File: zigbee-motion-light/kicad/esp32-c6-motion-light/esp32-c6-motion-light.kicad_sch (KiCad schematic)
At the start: 1 part, among them U1 XIAO-ESP32-C6-DIP

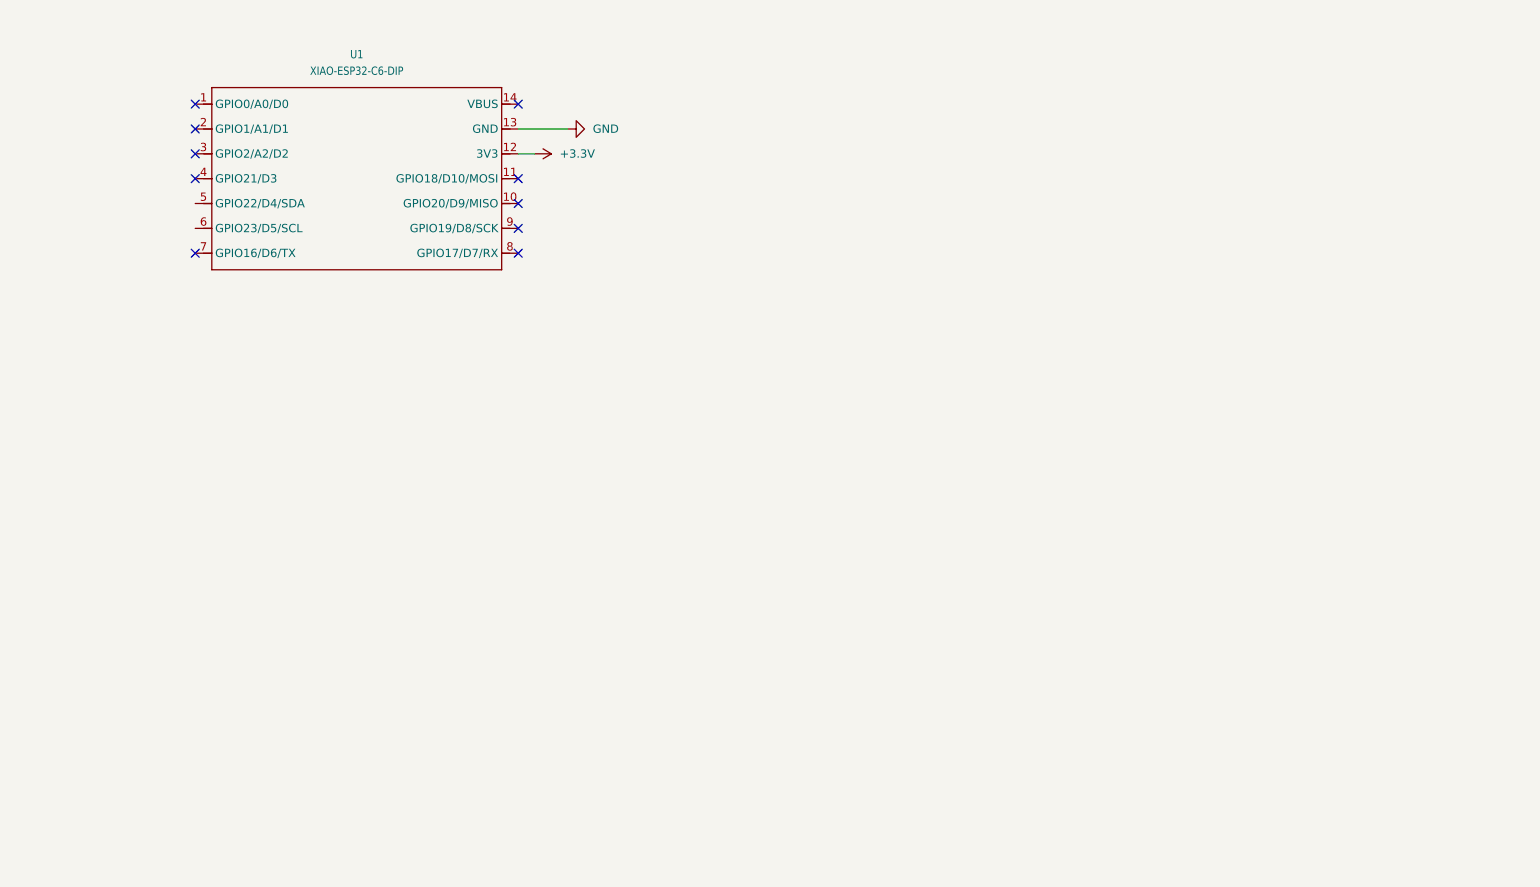
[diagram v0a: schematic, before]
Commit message: Add RP2040 component from EasyEDA and update KiCad project files
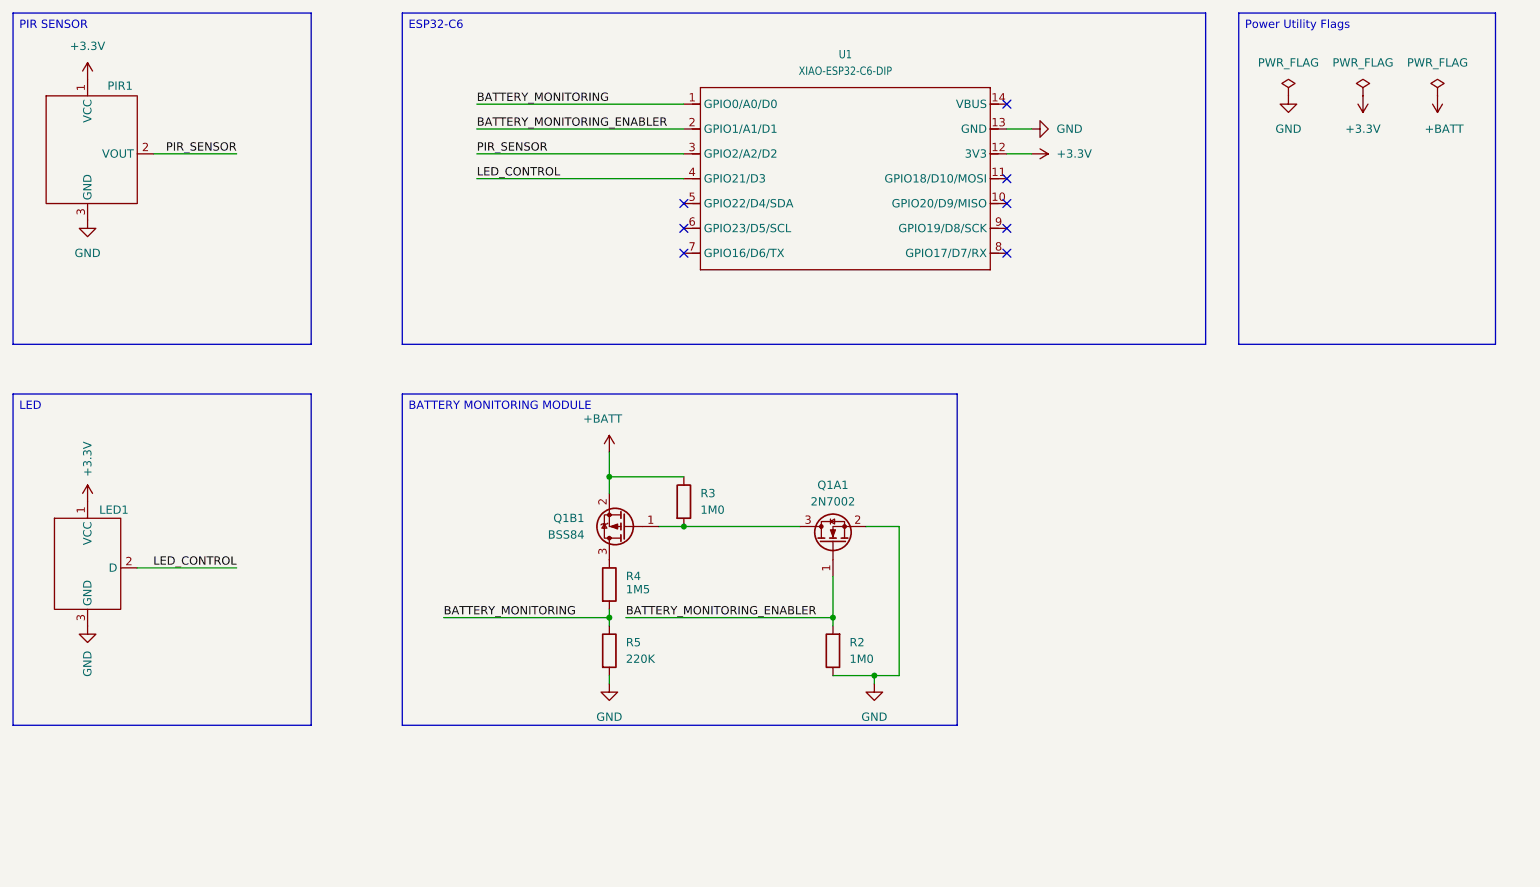
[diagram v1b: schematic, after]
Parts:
- added LED1: (no value), symbol New_Library:LED_CONNECTOR
- added PIR1: (no value), symbol New_Library:AM312_PIR
- added Q1A1: 2N7002, Package_TO_SOT_SMD:SOT-23, symbol Transistor_FET:2N7002
- added Q1B1: BSS84, Package_TO_SOT_SMD:SOT-23, symbol Transistor_FET:BSS84
- added R2, R3: 1M0, symbol Device:R
- added R4: 1M5, symbol Device:R
- added R5: 220K, symbol Device:R
- U1: footprint Library:XIAO-ESP32-C6-DIP -> seeds-studio:XIAO-ESP32-C6-DIP
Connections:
- net +3.3V: now also LED1.1 (VCC), PIR1.1 (VCC)
- net GND: now also LED1.3 (GND), PIR1.3 (GND), Q1A1.2 (S), R2.1, R5.2
- net BATTERY_MONITORING: now reaches U1.1 (GPIO0/A0/D0)
- net BATTERY_MONITORING: now also R4.2, R5.1
- net BATTERY_MONITORING_ENABLER: now reaches U1.2 (GPIO1/A1/D1)
- net BATTERY_MONITORING_ENABLER: now also Q1A1.1 (G), R2.2
- net PIR_SENSOR: now reaches U1.3 (GPIO2/A2/D2)
- net PIR_SENSOR: now also PIR1.2 (VOUT)
- net LED_CONTROL: now reaches U1.4 (GPIO21/D3)
- net LED_CONTROL: now also LED1.2 (D)
- new net: Q1B1.3 (D), R4.1
- new net: Q1A1.3 (D), Q1B1.1 (G), R3.2
- new net +BATT: Q1B1.2 (S), R3.1
- no-connect marks 10 -> 8
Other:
- company: (none) -> Ilia Kurgankii
- title: (none) -> ESP32-C6 Zigbee/Motion sensor
- moved on the sheet: U1

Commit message: Remove unused custom KiCAD footprints (SCD41-4pins and XIAO-ESP32-C6-DIP)
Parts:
- removed LED1: (no value), symbol New_Library:LED_CONNECTOR
- removed PIR1: (no value), symbol New_Library:AM312_PIR
- removed U1: XIAO-ESP32-C6-DIP, seeds-studio:XIAO-ESP32-C6-DIP, symbol seeds-studio:XIAO_ESP32-C6-DIP
- added LED1: (no value), Connector_PinHeader_1.00mm:PinHeader_1x03_P1.00mm_Vertical, symbol 1_custom:LED_CONNECTOR
- added PIR2: (no value), Connector_PinHeader_1.00mm:PinHeader_1x03_P1.00mm_Vertical, symbol 1_custom:AM312
- added U1: XIAO-ESP32-C6-DIP, 1_seeds-studio:XIAO-ESP32-S3-DIP, symbol 1_seeds-studio:XIAO_ESP32-C6-DIP
- Q1A1: footprint Package_TO_SOT_SMD:SOT-23 -> 1_easyeda2kicad:SOT-23-3_L2.9-W1.3-P1.90-LS2.4-BR
- Q1B1: footprint Package_TO_SOT_SMD:SOT-23 -> 1_easyeda2kicad:SOT-23-3_L3.0-W1.7-P0.95-LS2.9-BR
- R2, R3, R5: footprint (none) -> 1_easyeda2kicad:R0805
- R4: footprint (none) -> 1_easyeda2kicad:R0603
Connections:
- net +3.3V: now also LED1.1 (VCC), PIR2.1 (VCC), U1.12 (3V3)
- net BATTERY_MONITORING: now also U1.1 (GPIO0/A0/D0)
- net BATTERY_MONITORING_ENABLER: now also U1.2 (GPIO1/A1/D1)
- net GND: now also LED1.3 (GND), PIR2.3 (GND), U1.13 (GND)
- net LED_CONTROL: now also LED1.2 (DATA), U1.4 (GPIO21/D3)
- net PIR_SENSOR: now also PIR2.2 (OUT), U1.3 (GPIO2/A2/D2)

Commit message: feat: update kikad
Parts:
- added J1: Conn_01x02, Connector_JST:JST_XH_B2B-XH-A_1x02_P2.50mm_Vertical, symbol Connector_Generic:Conn_01x02
- added JP1: Enabled for Batter Monitoring, Jumper:SolderJumper-2_P1.3mm_Open_RoundedPad1.0x1.5mm, symbol Jumper:SolderJumper_2_Open
- added TP1: GND, TestPoint:TestPoint_Pad_2.0x2.0mm, symbol Connector:TestPoint
- added TP2: BATT+, TestPoint:TestPoint_Pad_2.0x2.0mm, symbol Connector:TestPoint
- added TP3: BATT-, TestPoint:TestPoint_Pad_2.0x2.0mm, symbol Connector:TestPoint
- added TP4: +3.3, TestPoint:TestPoint_Pad_2.0x2.0mm, symbol Connector:TestPoint
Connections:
- net +3.3V: now also TP4.1
- net +BATT: now also J1.2 (Pin_2), JP1.2 (B), TP2.1; no longer Q1B1.2 (S), R3.1
- net GND: now also TP1.1
- new net: JP1.1 (A), Q1B1.2 (S), R3.1
- new net -BATT: J1.1 (Pin_1), TP3.1
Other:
- moved on the sheet: Q1A1, Q1B1, R2, R3, R4, R5

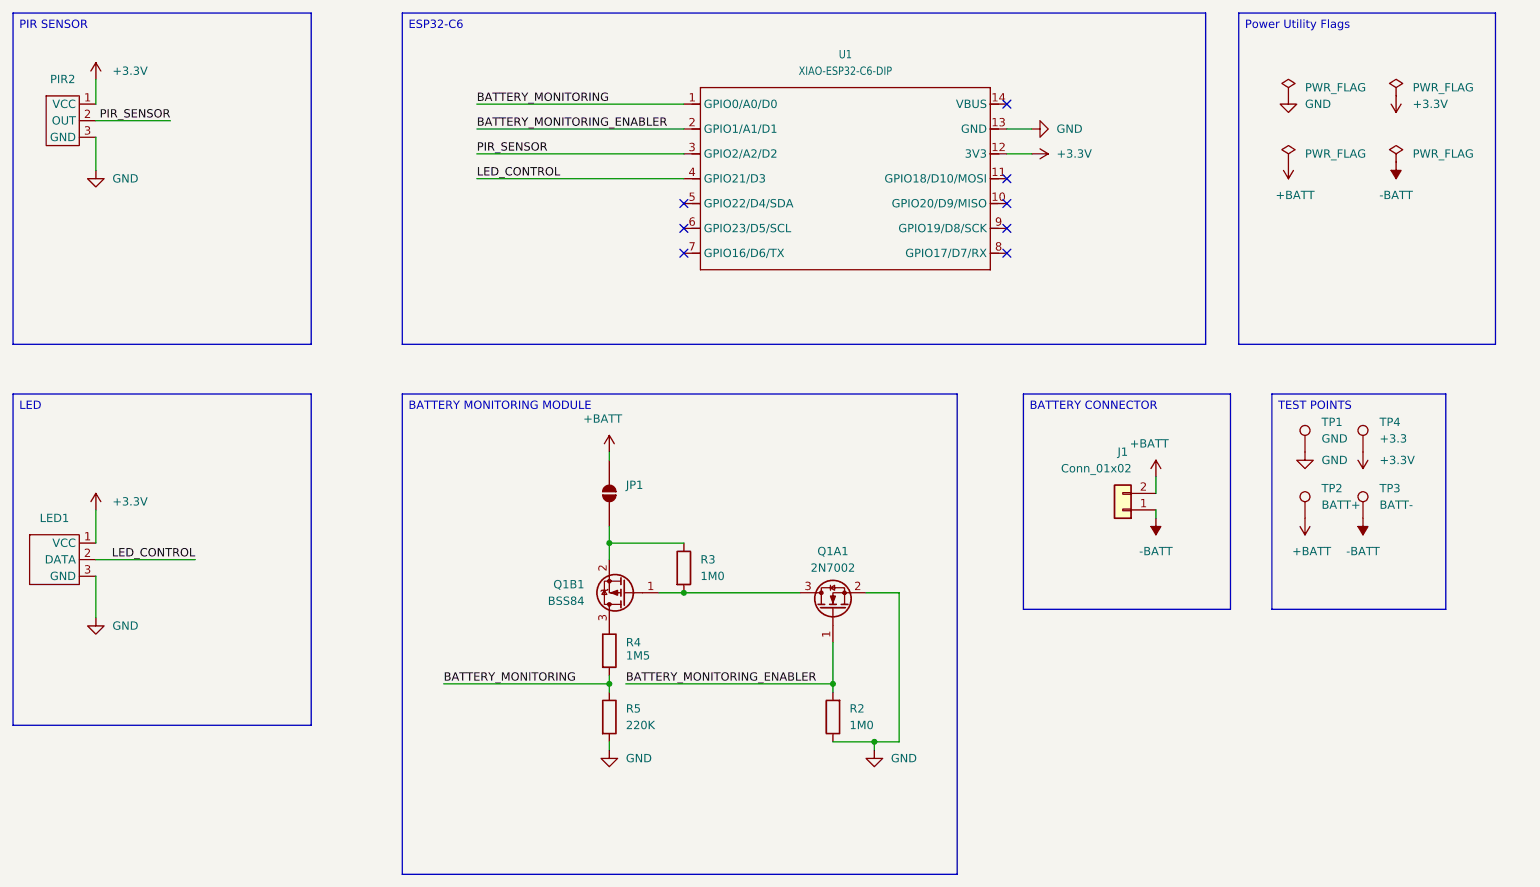
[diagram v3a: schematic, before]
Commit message: fix: wait for Zigbee join before deep sleep and fix task lifecycle
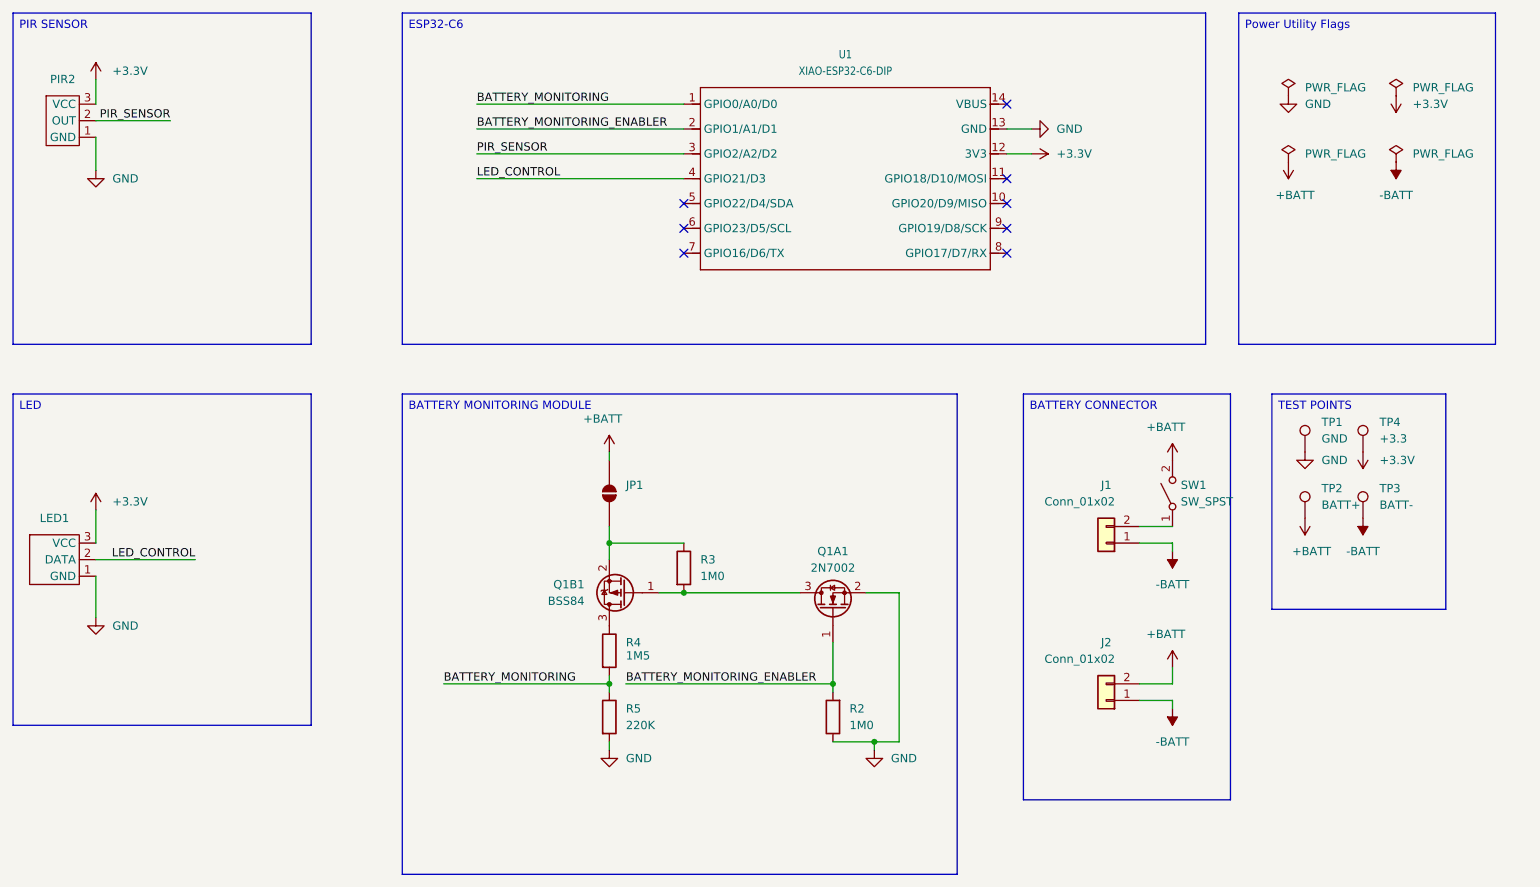
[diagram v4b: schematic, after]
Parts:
- added J2: Conn_01x02, Connector_JST:JST_XH_B2B-XH-A_1x02_P2.50mm_Vertical, symbol Connector_Generic:Conn_01x02
- added SW1: SW_SPST, Button_Switch_SMD:SW_SPDT_CK_JS102011SAQN, symbol Switch:SW_SPST
- LED1, PIR2: footprint Connector_PinHeader_1.00mm:PinHeader_1x03_P1.00mm_Vertical -> Connector_PinHeader_2.54mm:PinHeader_1x03_P2.54mm_Vertical
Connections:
- net +3.3V: now also LED1.3 (VCC), PIR2.3 (VCC); no longer LED1.1 (VCC), PIR2.1 (VCC)
- net +BATT: now also J2.2 (Pin_2), SW1.2 (B); no longer J1.2 (Pin_2)
- net -BATT: now also J2.1 (Pin_1)
- net GND: now also LED1.1 (GND), PIR2.1 (GND); no longer LED1.3 (GND), PIR2.3 (GND)
- new net: J1.2 (Pin_2), SW1.1 (A)
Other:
- moved on the sheet: J1

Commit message: update KiCAD files
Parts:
- SW1: footprint Button_Switch_SMD:SW_SPDT_CK_JS102011SAQN -> Connector_PinHeader_2.54mm:PinHeader_1x03_P2.54mm_Vertical
- TP1, TP2, TP3, TP4: footprint TestPoint:TestPoint_Pad_2.0x2.0mm -> TestPoint:TestPoint_THTPad_2.0x2.0mm_Drill1.0mm
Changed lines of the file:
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@@
 			)
 		)
-		(property "Footprint" "TestPoint:TestPoint_Pad_2.0x2.0mm"
+		(property "Footprint" "TestPoint:TestPoint_THTPad_2.0x2.0mm_Drill1.0mm"
 			(at 220.98 111.76 0)
 			(hide yes)
@@
 			)
 		)
-		(property "Footprint" "TestPoint:TestPoint_Pad_2.0x2.0mm"
+		(property "Footprint" "TestPoint:TestPoint_THTPad_2.0x2.0mm_Drill1.0mm"
 			(at 220.98 101.6 0)
 			(hide yes)
@@
 			)
 		)
-		(property "Footprint" "TestPoint:TestPoint_Pad_2.0x2.0mm"
+		(property "Footprint" "TestPoint:TestPoint_THTPad_2.0x2.0mm_Drill1.0mm"
 			(at 229.87 111.76 0)
 			(hide yes)
@@
 			)
 		)
-		(property "Footprint" "TestPoint:TestPoint_Pad_2.0x2.0mm"
+		(property "Footprint" "TestPoint:TestPoint_THTPad_2.0x2.0mm_Drill1.0mm"
 			(at 229.87 101.6 0)
 			(hide yes)
@@
 			)
 		)
-		(property "Footprint" "Button_Switch_SMD:SW_SPDT_CK_JS102011SAQN"
+		(property "Footprint" "Connector_PinHeader_2.54mm:PinHeader_1x03_P2.54mm_Vertical"
 			(at 195.58 107.95 0)
 			(hide yes)
